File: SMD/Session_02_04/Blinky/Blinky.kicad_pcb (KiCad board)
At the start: 2 copper layers, 30 x 30 mm, 12 parts, among them U1 TLC551CD‎

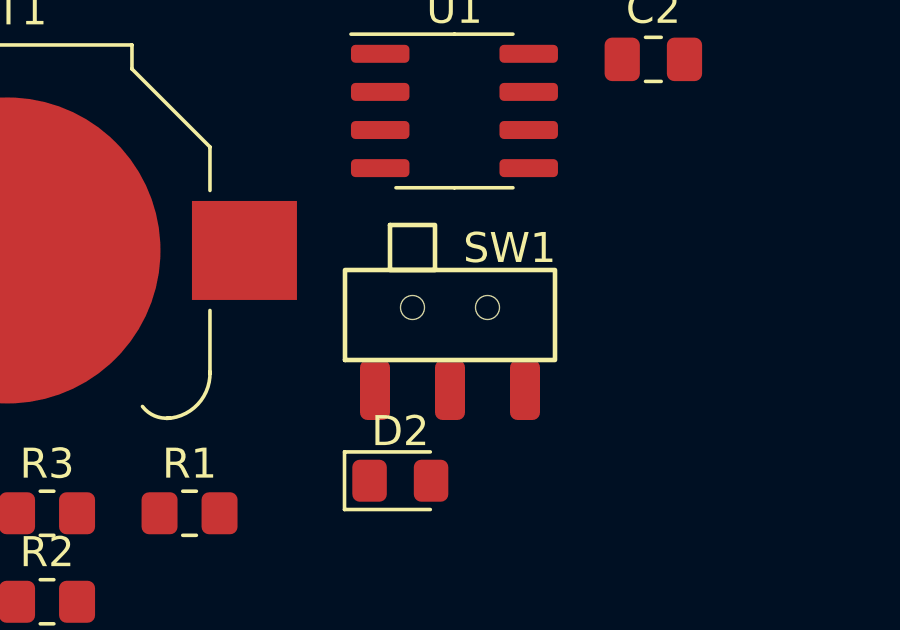
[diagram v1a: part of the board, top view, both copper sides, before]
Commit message: Corrections to the switch footprint
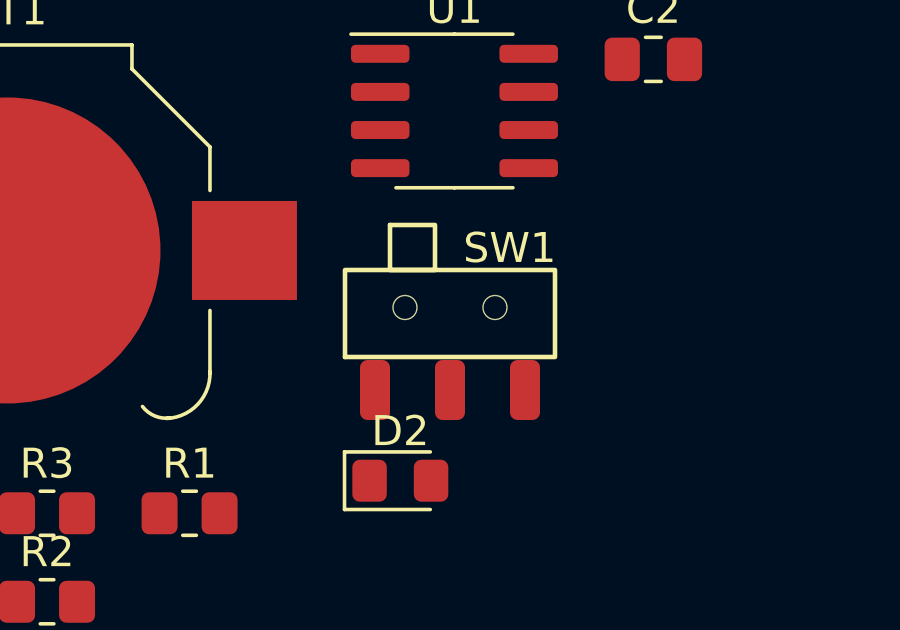
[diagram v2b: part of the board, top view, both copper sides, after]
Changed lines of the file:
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@@
       (effects (font (size 1 1) (thickness 0.15)))
     )
-    (fp_rect (start -3.500001 -1) (end 3.500001 -4) (layer "F.SilkS") (width 0.1524) (fill none))
+    (fp_rect (start -3.500001 -1.1) (end 3.500001 -4) (layer "F.SilkS") (width 0.1524) (fill none))
     (fp_rect (start -2 -5.499999) (end -0.5 -4) (layer "F.SilkS") (width 0.1524) (fill none))
     (fp_rect (start -3.5 -5.5) (end 3.5 1) (layer "F.CrtYd") (width 0.01) (fill none))
-    (pad "" np_thru_hole circle (at -1.25 -2.75) (size 0.8 0.8) (drill 0.8) (layers F&B.Cu *.Mask))
-    (pad "" np_thru_hole circle (at 1.25 -2.75) (size 0.8 0.8) (drill 0.8) (layers F&B.Cu *.Mask))
+    (pad "" np_thru_hole circle (at -1.5 -2.75) (size 0.8 0.8) (drill 0.8) (layers F&B.Cu *.Mask))
+    (pad "" np_thru_hole circle (at 1.5 -2.75) (size 0.8 0.8) (drill 0.8) (layers F&B.Cu *.Mask))
     (pad "1" smd roundrect (at -2.5 0) (size 1 2) (layers "F.Cu" "F.Paste" "F.Mask") (roundrect_rratio 0.25)
       (net 4 "Net-(C2-Pad1)") (pinfunction "A") (pintype "passive"))
